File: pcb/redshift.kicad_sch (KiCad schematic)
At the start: 75 parts, among them IC1 LPC5526JEV98, J1 USB_C_Receptacle_USB2.0, J2 Side, J3 Conn_01x06_Female, J4 Conn_ARM_JTAG_SWD_10, SW1 SW_SP, SW2 SW_SP, SW3 SW_SP, SW4 PTS810, U1 PAW3399DM‐T4QU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

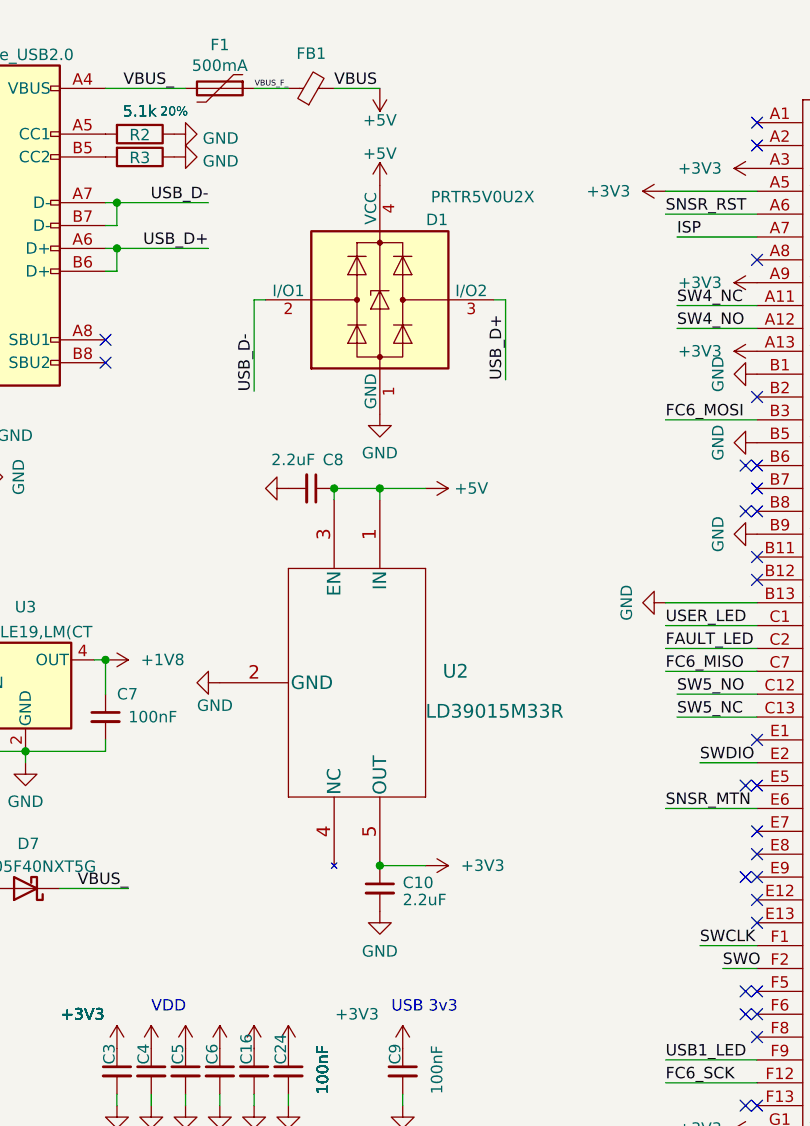
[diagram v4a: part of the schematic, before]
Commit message: Added cheap and slightly larger 3.3v LDO
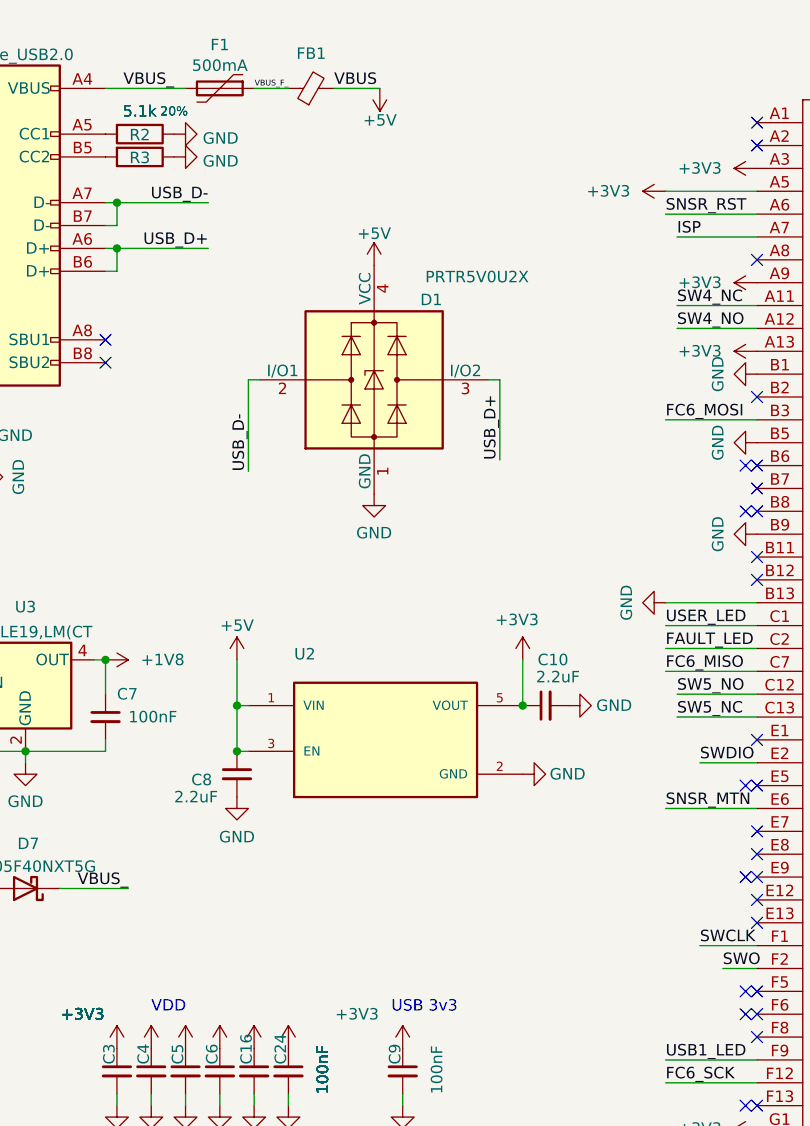
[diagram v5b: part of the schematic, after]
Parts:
- removed U2: LD39015M33R, symbol LD39015M33R:LD39015M33R
- added U2: (no value), symbol MIC5365-3.3YC5-TR:MIC5365-3.3YC5-TR
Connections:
- net +3V3: now also U2.5 (VOUT)
- net +5V: now also U2.1 (VIN), U2.3 (EN)
- net GND: now also U2.2 (GND)
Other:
- moved on the sheet: C10, C8, D1

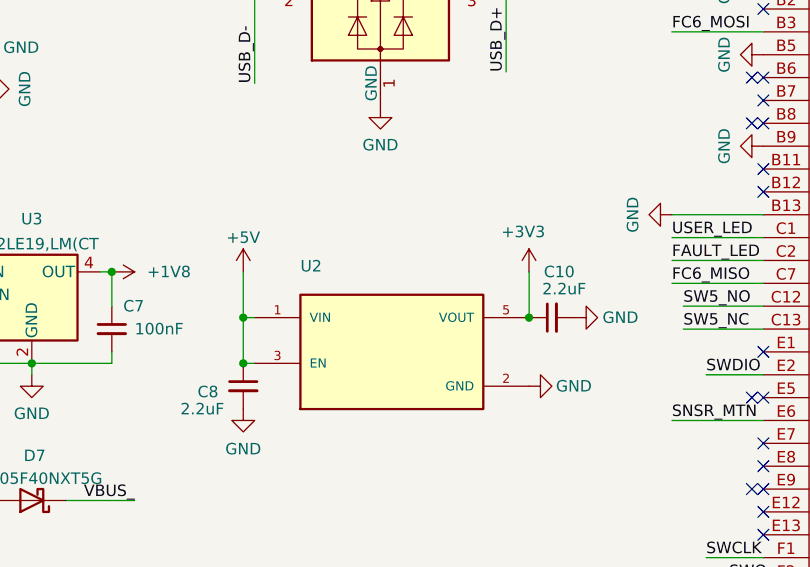
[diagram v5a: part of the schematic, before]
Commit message: Added the only missing lib I could find: the mcu
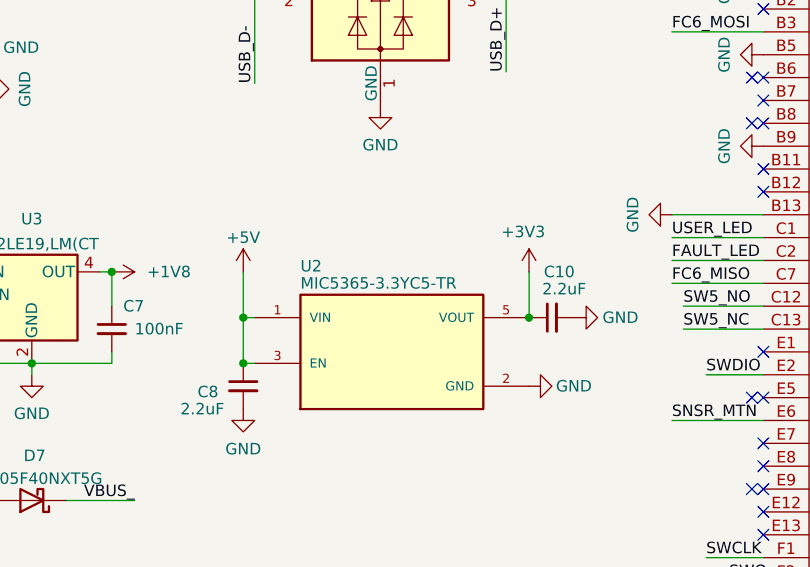
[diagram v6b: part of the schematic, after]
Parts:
- U2: value (none) -> MIC5365-3.3YC5-TR; footprint (none) -> MIC5365-3.3YC5-TR:SOT65P210X110-5N

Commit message: First
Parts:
- removed D5: RED, LED_SMD:LED_0402_1005Metric, symbol Device:LED_Small
- removed R7: 10k, Resistor_SMD:R_0402_1005Metric, symbol Device:R_Small
- added C?: 10uF, Capacitor_SMD:C_0402_1005Metric, symbol Device:C_Small
- added R?: 9.31+-1%, symbol Device:R_Small
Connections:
- net +1V8: now also C19.1, C20.1, U1.4 (VDD); no longer C19.2, C20.2
- net +3V3: now also C17.2, C18.2, U1.7 (VDDIO); no longer C17.1, C18.1
- net GND: now also C17.1, C18.1, C19.2, C20.2, C?.1, R?.1
- net SNSR_LED: no longer names the net of U1.15 (LED_P)
- net SNSR_LED: now also R?.2

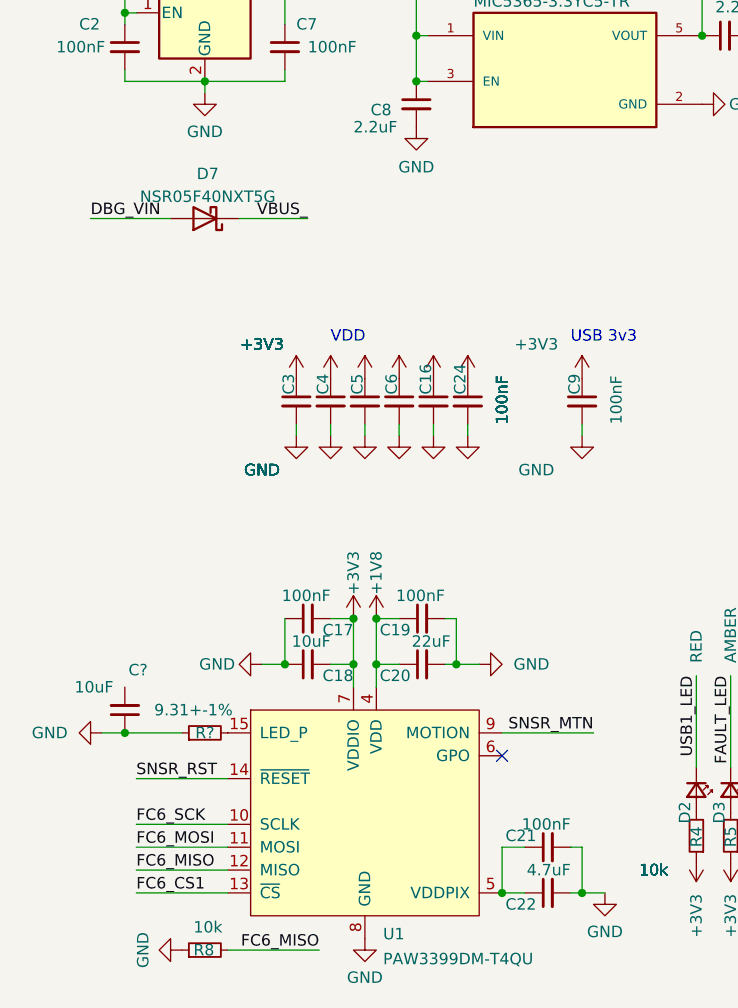
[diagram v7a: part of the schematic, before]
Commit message: Fixed VDD/IO, LED_P, and removed Sensor LED from Schematic
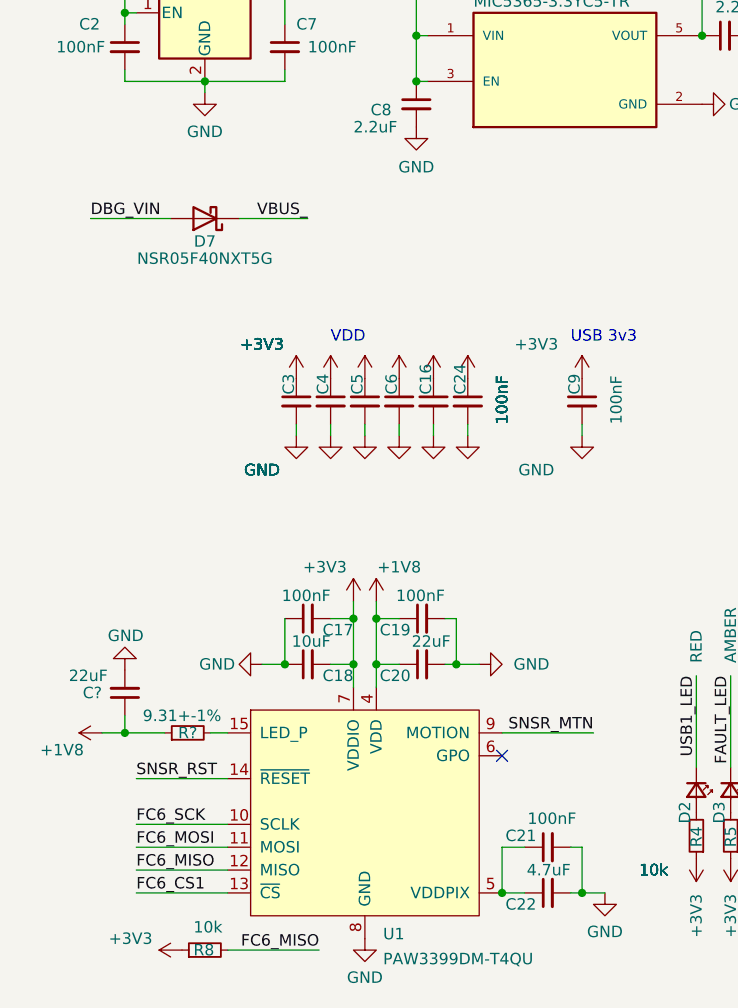
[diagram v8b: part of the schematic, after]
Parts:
- C?: value 10uF -> 22uF
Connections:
- net +1V8: now also C?.1, R?.1
- net +3V3: now also R8.1
- net GND: now also C?.2; no longer C?.1, R8.1, R?.1
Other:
- moved on the sheet: C?, R?
